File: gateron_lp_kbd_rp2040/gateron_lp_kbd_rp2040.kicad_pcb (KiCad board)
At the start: 4 copper layers, 234.5 x 116.5 mm, 306 parts, among them J1 TYPE-C-31-M-12, J2 Battery JST-SH, Q1 DMG3415U, SW1 KS-33, SW10 KS-33, SW11 KS-33, SW12 KS-33, SW13 KS-33, SW14 KS-33, SW15 KS-33, SW16 KS-33, SW17 KS-33, SW18 KS-33, SW19 KS-33, SW2 KS-33, SW20 KS-33, SW21 KS-33, SW22 KS-33, SW23 KS-33, SW24 KS-33, SW25 KS-33, SW26 KS-33, SW27 KS-33, SW28 KS-33, SW29 KS-33, SW3 KS-33, SW30 KS-33, SW31 KS-33, SW32 KS-33, SW33 KS-33, SW34 KS-33, SW35 KS-33, SW36 KS-33, SW37 KS-33, SW38 KS-33, SW39 KS-33, SW4 KS-33, SW40 KS-33, SW41 KS-33, SW42 KS-33, SW43 KS-33, SW44 KS-33, SW45 KS-33, SW46 KS-33, SW47 KS-33, SW48 KS-33, SW49 KS-33, SW5 KS-33, SW50 KS-33, SW51 KS-33, SW52 KS-33, SW53 KS-33, SW54 KS-33, SW55 KS-33, SW56 KS-33, SW57 KS-33, SW58 KS-33, SW59 KS-33, SW6 KS-33, SW60 RESET, SW61 BOOTSEL, SW62 PWR MSK-12C02, SW7 KS-33, SW8 KS-33, SW9 KS-33, U1 RP2040, U2 MCP73831, U3 AP2112K-3.3, U4 USBLC6-2SC6, U5 W25Q16JVUXIQ, U6 CYW43439, U7 SN74AHCT1G125DBVR, Y1 12MHz, Y2 37.4MHz

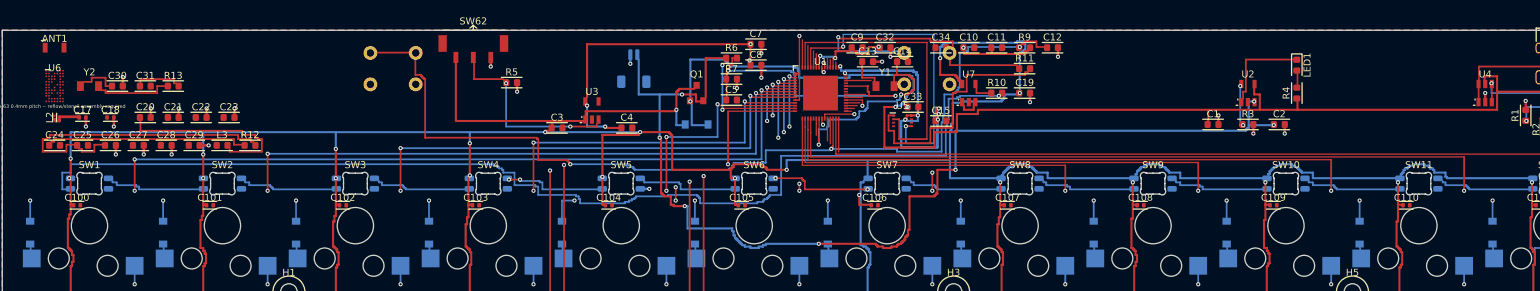
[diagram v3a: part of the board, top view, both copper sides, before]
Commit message: Fix pin10's escape wall trapping QSPI_SS; document XIN/pin42 conflict
Pin 10's original escape via (found 9.2mm due north) built a long
F-layer wall that boxed in QSPI_SS's escape stub and shrank XIN's
routing pocket. Rerouted pin 10 south instead (2.5mm via vs. 9.2mm),
clear of both. QSPI_SS now routes and heals cleanly.

XIN still conflicts with +3V3 pin 42: tested half a dozen alternate
via positions for pin 42 across a 3mm arc, and reordering XIN before
the +3V3/DVDD block entirely (which just pushes an equivalent failure
onto DVDD pin 23 instead) -- this pocket between U1's crystal and the
QSPI/BOOTSEL cluster is genuinely oversaturated, matching the already-
documented QSPI_SCLK/SD2/SD3/VREG_VIN/RGB_GPIO failures in the same
neighborhood. +3V3 pin 42 (real board power) wins; XIN is left for
manual routing in KiCad, same as those other nets.

VSYS's own heal failure is confirmed pre-existing (present even at the
bd09c6a baseline before any of this +3V3/DVDD work) -- not a
regression from this refactor, left untouched.

Co-Authored-By: Claude Sonnet 5 <noreply@anthropic.com>
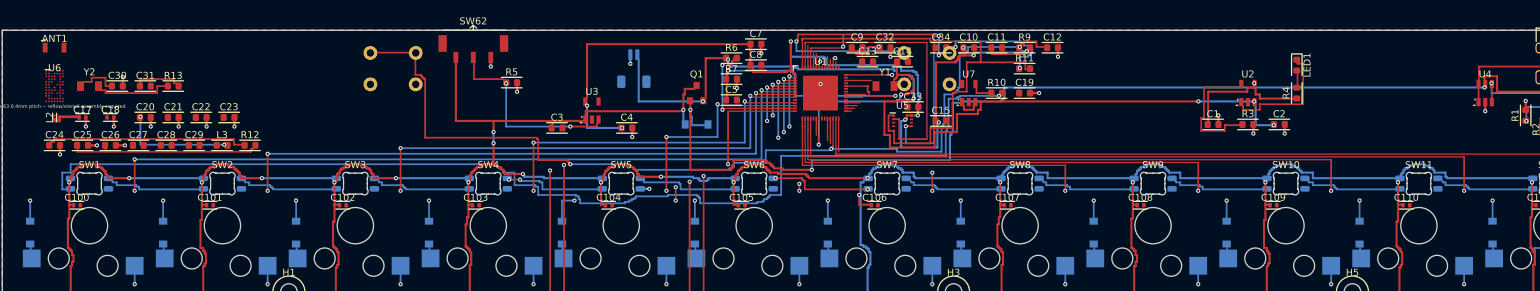
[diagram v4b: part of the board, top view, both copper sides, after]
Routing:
- net +3V3: track 235.3 -> 151.0 mm, vias 17 -> 10
- net VSYS: track 1512.8 -> 1444.5 mm, vias 69 -> 68
- net QSPI_SS: track 39.1 -> 71.1 mm
- net BAT+: track 157.2 -> 133.0 mm, vias 7 -> 6
- net BOOTSEL: track 41.5 -> 61.9 mm, vias 1 -> 5
- net CYW_PA_VDD: track 45.0 -> 27.9 mm
- net PROG: track 6.13 -> 18.7 mm, vias 2 -> 0
- net CYW_VDD1P5: track 27.5 -> 16.3 mm, vias 0 -> 2
- net XIN: track 7.30 -> 2.40 mm
- net STAT: track 13.5 -> 17.3 mm
- net VBUS: track 189.1 -> 186.7 mm, vias 2 -> 4
- net GND: track 59.9 -> 58.1 mm, vias 43 -> 42
- net DVDD: track 47.3 -> 48.4 mm, vias 5 -> 3

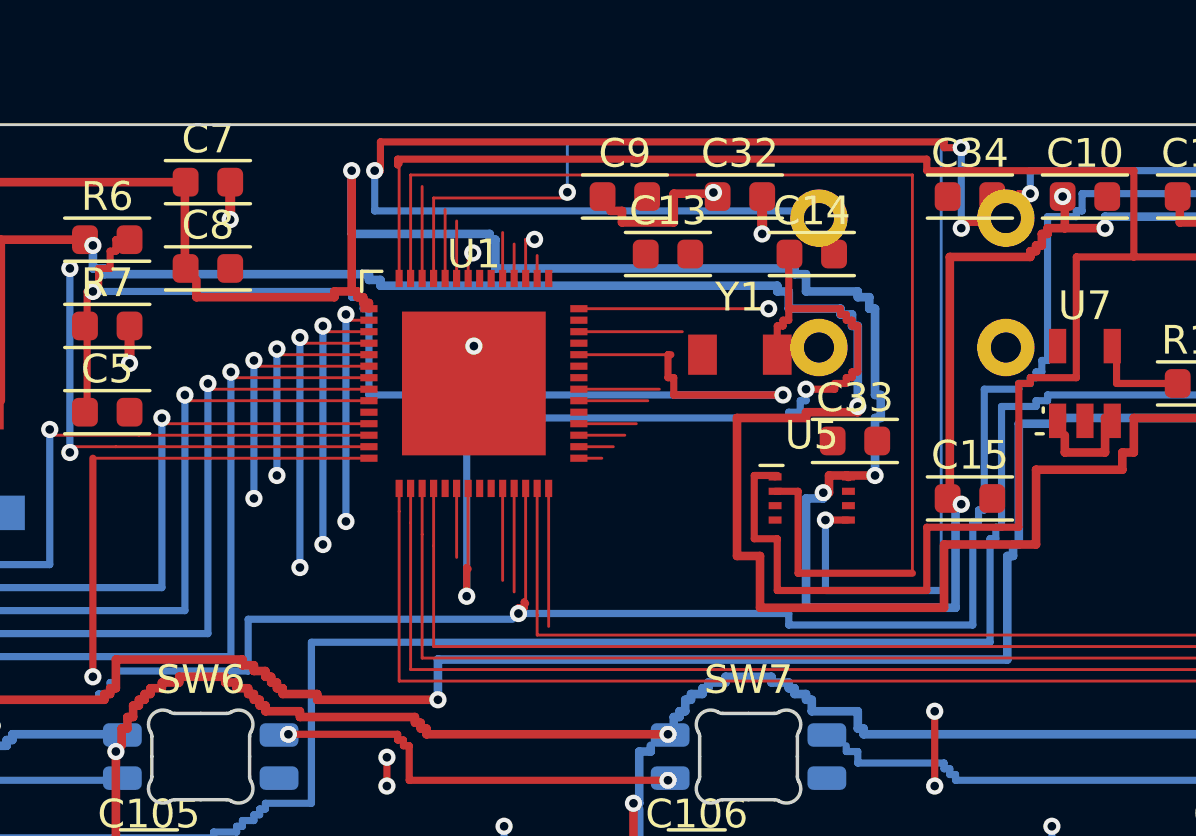
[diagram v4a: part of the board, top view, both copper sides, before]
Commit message: Investigate QSPI_SD2/SCLK/SD3 via In1/In2 expressways; no net change
Attempted the same In1/In2 expressway technique that fixed +3V3/DVDD
for these three QSPI flash data lines. QSPI_SCLK alone can be routed
this way (via a detour around BOOTSEL's two leg keepouts, QSPI_SD0's
own via/descent, and +3V3 pin 42's own In2 crossing), but SD2/SD3
cannot -- every via candidate east of +3V3 pin 10's own In2 wall sits
in a pocket boxed in by QSPI_SD0/SCLK's F escapes, USB_DP's F escape,
the raw N-side pin row, +3V3 pin 22/42's own In2 paths, and GND's
large pad.

Worse, SCLK's own fix needs enough of this same neighborhood that it
breaks BOOTSEL's and DVDD's already-working routes -- fixing one QSPI
data line at the cost of a button and core power, with no complete
QSPI interface anyway since SD2/SD3 (needed for quad-mode) still
wouldn't route. Reverted to the stable all-3-skipped state.

Promoted _find_via/_highway (used for the +3V3/DVDD fixes) from
run_routes()-local closures to module-level functions, with new
x_min/y_min filters for excluding known dead-end search directions --
no behavior change, verified identical output before this session's
QSPI investigation.

Co-Authored-By: Claude Sonnet 5 <noreply@anthropic.com>
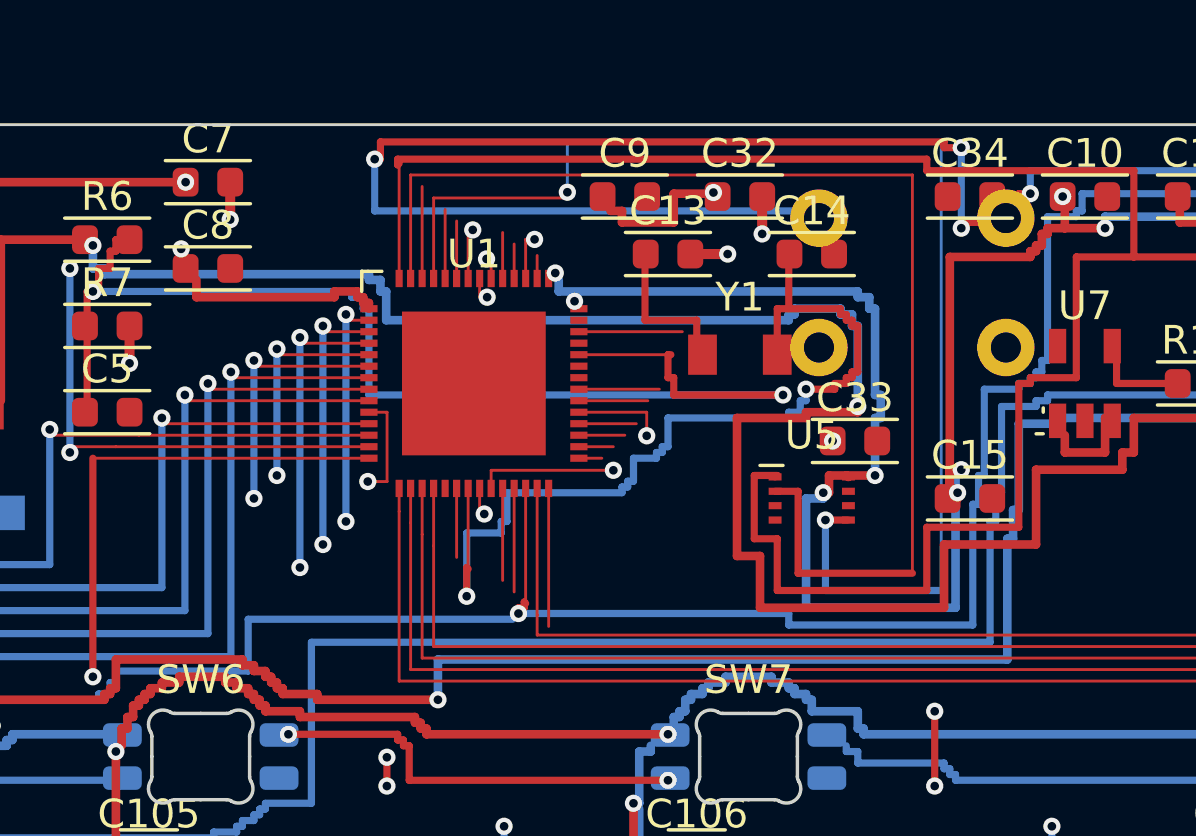
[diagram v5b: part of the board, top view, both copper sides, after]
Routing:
- net +3V3: track 151.0 -> 223.8 mm, vias 10 -> 18
- net DVDD: track 48.4 -> 62.0 mm, vias 3 -> 5
- net XIN: track 2.40 -> 7.30 mm
- net BAT+: track 133.0 -> 133.8 mm

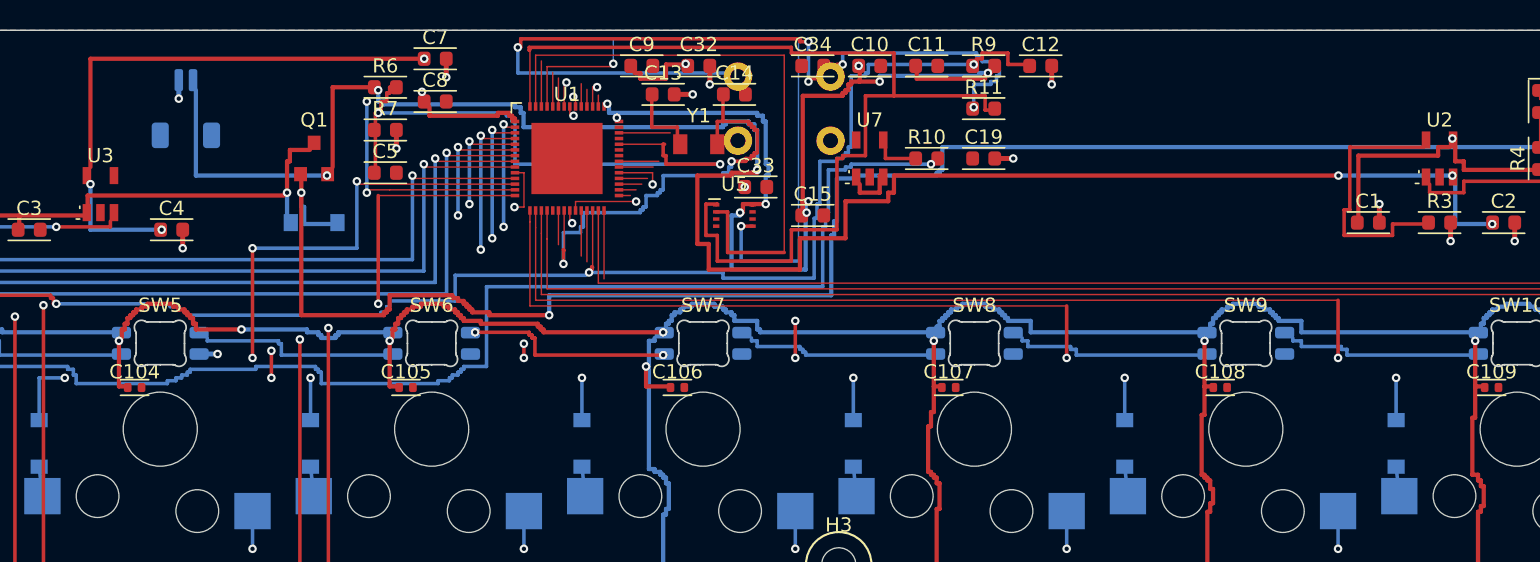
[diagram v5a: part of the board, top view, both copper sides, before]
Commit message: Fix RGB_GPIO's escape route past COL11's trunk trace
RGB_GPIO's escape stub ran parallel and immediately adjacent to
COL11's own trunk trace for its entire length (both are consecutive
S-side escape_fan pins at 0.4mm pitch) -- two normal-width (0.25mm)
traces need 0.45mm pitch to coexist, so the router could never widen
out from the narrow escape stub anywhere along its length. Confirmed
via astar()'s own source-seeding: every cell on RGB_GPIO's existing
escape stub fell inside COL11's clearance zone.

Fixed with a manual jog east (past COL11's vertical stub) and
slightly north to y=39.3 -- not y=39.45 (the escape stub's own
depth), which sits exactly 0.3mm from COL11's y=39.75 matrix trunk, a
floating-point tie at the clearance boundary that fails in practice.

RGB_GPIO now routes and heals cleanly with no regressions elsewhere;
verified deterministic across repeated runs.

Co-Authored-By: Claude Sonnet 5 <noreply@anthropic.com>
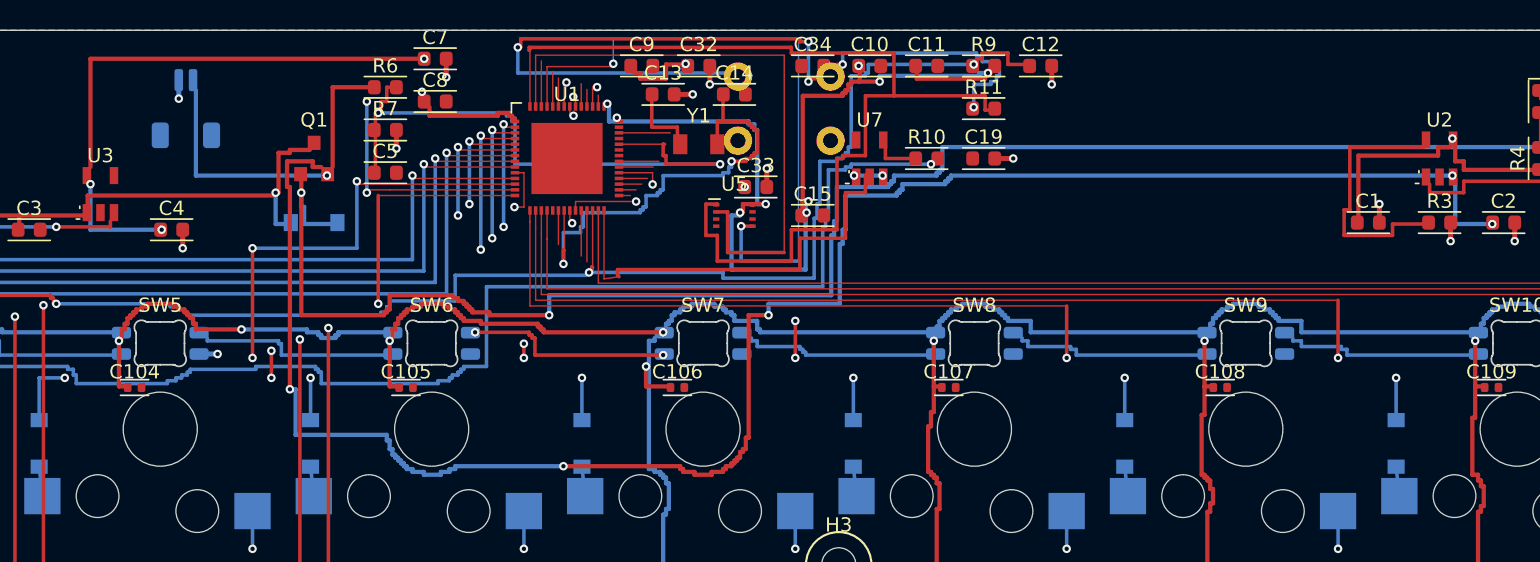
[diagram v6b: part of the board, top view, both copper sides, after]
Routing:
- net RGB_GPIO: track 4.80 -> 30.7 mm
- net BAT+: track 133.8 -> 158.8 mm
- net VSYS: track 1444.5 -> 1445.3 mm
- net GND: track 58.1 -> 58.0 mm, vias 42 -> 45

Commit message: Partially fix VREG_VIN's escape; document the remaining wall
VREG_VIN's escape point sat only 0.567mm from DVDD's own via
(part of the pin 45/50 -> C33 gather fix), closer than the 0.625mm a
normal-width departure needs -- the A* search couldn't leave its own
escape point at all. Fixed with a short jog east, still at the escape
stub's own narrow width, clearing the via with room to spare.

Past that, VREG_VIN still can't reach C34: x=161 is a solid wall from
y=23 to y=32, stacked from several different nets' own copper
(QSPI_SS/SD1, a DVDD crossing, XIN's own pad+wall, and the E-side
BT_*/VBAT_SENSE escape_fan cluster). The only clear crossings found
sit south of VREG_VIN's own reachable pocket, and a straight run down
to them hits BT_REG_ON's own raw pad directly. Left unrouted, same
oversaturated-neighborhood story as QSPI_SCLK/SD2/SD3.

No regressions: identical failure list elsewhere, verified
deterministic across repeated runs.

Co-Authored-By: Claude Sonnet 5 <noreply@anthropic.com>
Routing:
- net VREG_VIN: track 0.80 -> 1.85 mm
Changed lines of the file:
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@@
   (segment (start 154.710 23.700) (end 163.080 23.700) (width 0.3) (layer "In1.Cu") (net 18))
   (segment (start 163.080 23.700) (end 163.080 23.500) (width 0.3) (layer "In1.Cu") (net 18))
+  (segment (start 156.950 26.550) (end 158.000 26.550) (width 0.1) (layer "F.Cu") (net 17))
   (segment (start 157.350 39.450) (end 158.400 39.300) (width 0.1) (layer "F.Cu") (net 51))
   (segment (start 158.400 39.300) (end 158.300 39.200) (width 0.25) (layer "F.Cu") (net 51))

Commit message: Partially fix USB_DM's escape; document the long-haul NOVIA blocker
USB_DM's escape point couldn't depart at normal width: 0.4mm from
USB_DP's own parallel escape stub (same 0.4mm-pitch neighbor problem
as everywhere else on U1), and a straight jog east crossed DVDD's own
escape stub. Fixed with a jog north (clear of DVDD's stub) then east.

Neither USB_DM nor USB_DP can complete the ~90mm long-haul hop to U4
near the USB connector, though. Root-caused via astar()'s own
source-item seeding: the whole neighborhood around U1's N-side escape
cluster is only reachable via B layer (F is blocked solid by DVDD/
XIN/QSPI/BOOTSEL geometry), but it also sits inside
U1_ESCAPE_NOVIA (143-165, 24-38), where generic A* is barred from
creating a via by design. Manually placing that via (bypassing the
policy, as done for +3V3/DVDD/QSPI elsewhere) doesn't help either --
every candidate landing point just past the zone boundary is itself
blocked by a different net's own via or wall (BOOTSEL's keepout,
XOUT's pad, DVDD's pin-23 via, QSPI_SD0's own B-layer elevator).

No regressions: identical failure list elsewhere, verified
deterministic across repeated runs.

Co-Authored-By: Claude Sonnet 5 <noreply@anthropic.com>
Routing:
- net USB_DM: track 23.8 -> 27.4 mm
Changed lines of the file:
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@@
   (segment (start 257.900 37.000) (end 258.700 37.000) (width 0.25) (layer "F.Cu") (net 11))
   (segment (start 258.800 36.975) (end 258.700 37.000) (width 0.25) (layer "F.Cu") (net 11))
+  (segment (start 156.150 26.150) (end 156.150 25.400) (width 0.1) (layer "F.Cu") (net 9))
+  (segment (start 156.150 25.400) (end 159.000 25.400) (width 0.1) (layer "F.Cu") (net 9))
   (segment (start 249.900 30.200) (end 181.100 30.200) (width 0.3) (layer "B.Cu") (net 3))
   (segment (start 181.100 30.200) (end 181.100 31.800) (width 0.3) (layer "B.Cu") (net 3))
